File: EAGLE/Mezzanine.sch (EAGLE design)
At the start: 11 parts

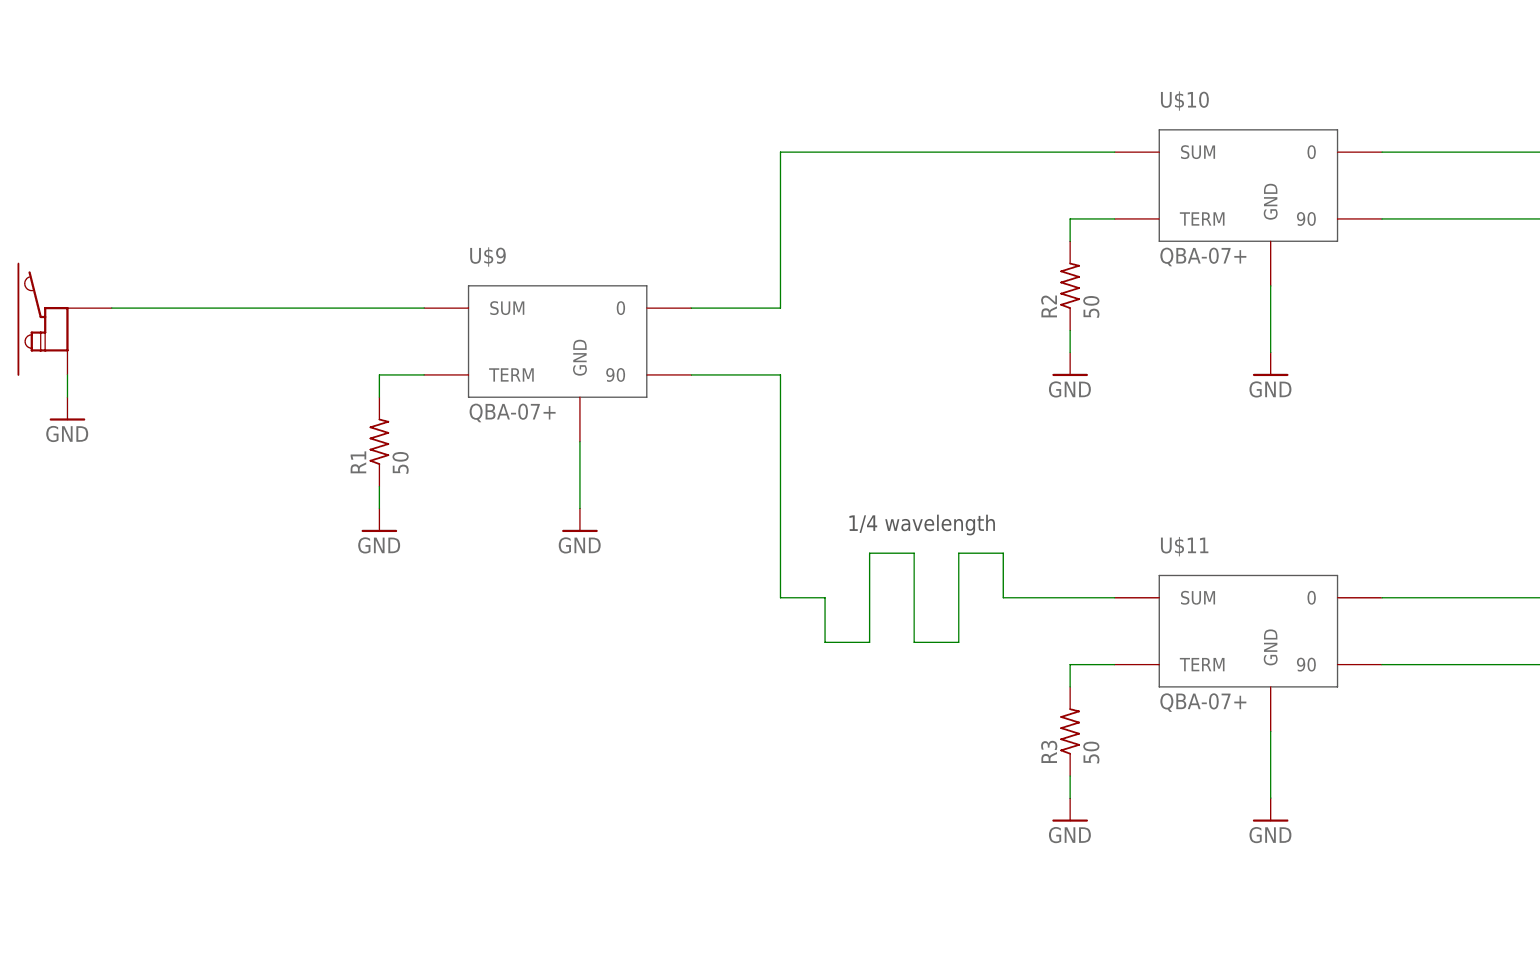
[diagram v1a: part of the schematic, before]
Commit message: Updated QBA footprints to have no solder mask in order to generate the correct solder paste stencils.
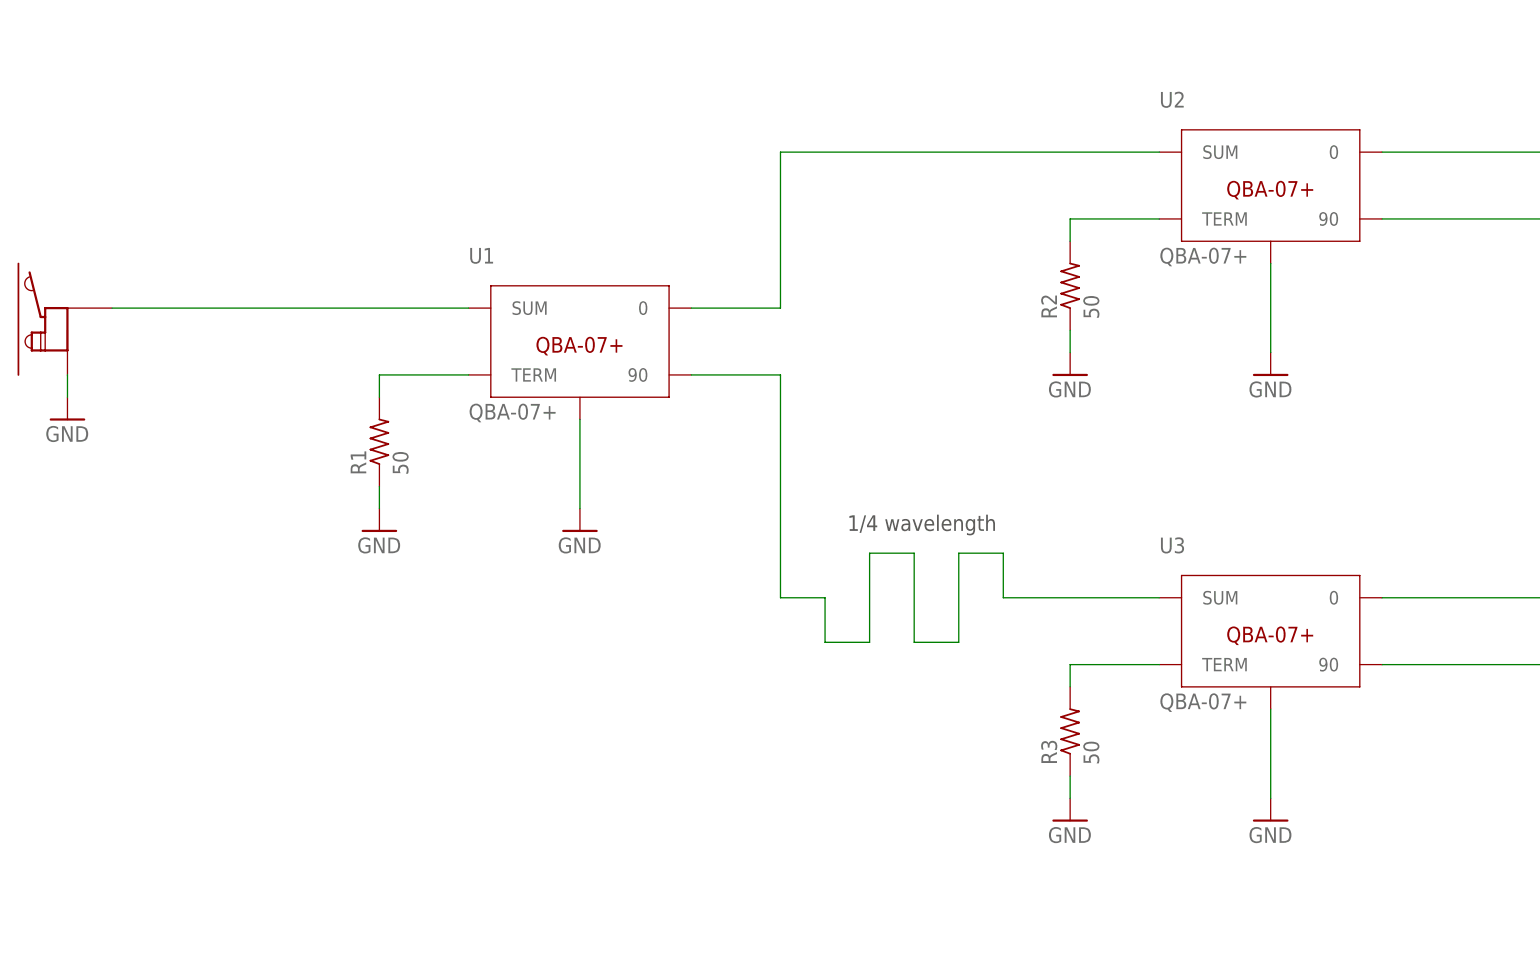
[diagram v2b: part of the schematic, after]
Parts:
- removed U$10, U$11, U$9: QBA-07+, Mini-Circuits-QBA-07+_Phase-shifter:QBA-07+
- added U1, U2, U3: QBA-07+, U-MiniCirc-QBA-07+_Phase-shifter:QBA-07+
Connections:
- net GND: now also U1.GND, U2.GND, U3.GND; no longer U$10.GND, U$11.GND, U$9.GND
- net N$1: now also U1.SUM; no longer U$9.SUM
- net N$2: now also U1.0, U2.SUM; no longer U$10.SUM, U$9.0
- net N$3: now also U1.TERM; no longer U$9.TERM
- net N$4: now also U2.TERM; no longer U$10.TERM
- net N$5: now also U1.90, U3.SUM; no longer U$11.SUM, U$9.90
- net N$6: now also U3.TERM; no longer U$11.TERM
- net UHF_0: now also U2.0; no longer U$10.0
- net UHF_180: now also U3.0; no longer U$11.0
- net UHF_270: now also U3.90; no longer U$11.90
- net UHF_90: now also U2.90; no longer U$10.90
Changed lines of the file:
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@@
 <?xml version="1.0" encoding="utf-8"?>
 <!DOCTYPE eagle SYSTEM "eagle.dtd">
-<eagle version="9.6.2">
+<eagle version="9.6.1">
 <drawing>
 <settings>
@@
 <parts>
 <part name="FRAME1" library="frames" library_urn="urn:adsk.eagle:library:229" deviceset="FRAME_A_L" device=""/>
-<part name="U$9" library="Mini-Circuits-QBA-07+_Phase-shifter" deviceset="QBA-07+" device=""/>
-<part name="U$10" library="Mini-Circuits-QBA-07+_Phase-shifter" deviceset="QBA-07+" device=""/>
-<part name="U$11" library="Mini-Circuits-QBA-07+_Phase-shifter" deviceset="QBA-07+" device=""/>
+<part name="U1" library="U-MiniCirc-QBA-07+_Phase-shifter" deviceset="QBA-07+" device=""/>
+<part name="U2" library="U-MiniCirc-QBA-07+_Phase-shifter" deviceset="QBA-07+" device=""/>
+<part name="U3" library="U-MiniCirc-QBA-07+_Phase-shifter" deviceset="QBA-07+" device=""/>
 <part name="GND1" library="supply1" library_urn="urn:adsk.eagle:library:371" deviceset="GND" device=""/>
 <part name="GND2" library="supply1" library_urn="urn:adsk.eagle:library:371" deviceset="GND" device=""/>
@@
 <attribute name="DRAWING_NAME" x="190.5" y="19.05" size="2.54" layer="94"/>
 </instance>
-<instance part="U$9" gate="G$1" x="91.44" y="127" smashed="yes">
+<instance part="U1" gate="G$1" x="91.44" y="127" smashed="yes">
 <attribute name="NAME" x="78.74" y="134.62" size="1.778" layer="95"/>
 <attribute name="VALUE" x="78.74" y="116.84" size="1.778" layer="96"/>
 </instance>
-<instance part="U$10" gate="G$1" x="170.18" y="144.78" smashed="yes">
+<instance part="U2" gate="G$1" x="170.18" y="144.78" smashed="yes">
 <attribute name="NAME" x="157.48" y="152.4" size="1.778" layer="95"/>
 <attribute name="VALUE" x="157.48" y="134.62" size="1.778" layer="96"/>
 </instance>
-<instance part="U$11" gate="G$1" x="170.18" y="93.98" smashed="yes">
+<instance part="U3" gate="G$1" x="170.18" y="93.98" smashed="yes">
 <attribute name="NAME" x="157.48" y="101.6" size="1.778" layer="95"/>
 <attribute name="VALUE" x="157.48" y="83.82" size="1.778" layer="96"/>
@@
 <net name="N$1" class="1">
 <segment>
-<pinref part="U$9" gate="G$1" pin="SUM"/>
-<wire x1="38.1" y1="129.54" x2="73.66" y2="129.54" width="0.1524" layer="91"/>
+<pinref part="U1" gate="G$1" pin="SUM"/>
+<wire x1="38.1" y1="129.54" x2="78.74" y2="129.54" width="0.1524" layer="91"/>
 <pinref part="U$1" gate="G$1" pin="P$1"/>
 </segment>
@@
 <net name="N$2" class="1">
 <segment>
-<pinref part="U$9" gate="G$1" pin="0"/>
+<pinref part="U1" gate="G$1" pin="0"/>
 <wire x1="104.14" y1="129.54" x2="114.3" y2="129.54" width="0.1524" layer="91"/>
 <wire x1="114.3" y1="129.54" x2="114.3" y2="147.32" width="0.1524" layer="91"/>
-<pinref part="U$10" gate="G$1" pin="SUM"/>
-<wire x1="114.3" y1="147.32" x2="152.4" y2="147.32" width="0.1524" layer="91"/>
+<pinref part="U2" gate="G$1" pin="SUM"/>
+<wire x1="114.3" y1="147.32" x2="157.48" y2="147.32" width="0.1524" layer="91"/>
 </segment>
 </net>
 <net name="N$3" class="1">
 <segment>
-<pinref part="U$9" gate="G$1" pin="TERM"/>
-<wire x1="73.66" y1="121.92" x2="68.58" y2="121.92" width="0.1524" layer="91"/>
+<pinref part="U1" gate="G$1" pin="TERM"/>
+<wire x1="78.74" y1="121.92" x2="68.58" y2="121.92" width="0.1524" layer="91"/>
 <wire x1="68.58" y1="121.92" x2="68.58" y2="119.38" width="0.1524" layer="91"/>
 <pinref part="R1" gate="R" pin="2"/>
@@
 </segment>
 <segment>
-<pinref part="U$9" gate="G$1" pin="GND"/>
+<pinref part="U1" gate="G$1" pin="GND"/>
 <pinref part="GND1" gate="1" pin="GND"/>
-<wire x1="91.44" y1="114.3" x2="91.44" y2="106.68" width="0.1524" layer="91"/>
-</segment>
-<segment>
-<pinref part="U$10" gate="G$1" pin="GND"/>
+<wire x1="91.44" y1="116.84" x2="91.44" y2="106.68" width="0.1524" layer="91"/>
+</segment>
+<segment>
+<pinref part="U2" gate="G$1" pin="GND"/>
 <pinref part="GND2" gate="1" pin="GND"/>
-<wire x1="170.18" y1="132.08" x2="170.18" y2="124.46" width="0.1524" layer="91"/>
+<wire x1="170.18" y1="134.62" x2="170.18" y2="124.46" width="0.1524" layer="91"/>
 </segment>
 <segment>
@@
 </segment>
 <segment>
-<pinref part="U$11" gate="G$1" pin="GND"/>
+<pinref part="U3" gate="G$1" pin="GND"/>
 <pinref part="GND3" gate="1" pin="GND"/>
-<wire x1="170.18" y1="81.28" x2="170.18" y2="73.66" width="0.1524" layer="91"/>
+<wire x1="170.18" y1="83.82" x2="170.18" y2="73.66" width="0.1524" layer="91"/>
 </segment>
 <segment>
@@
 <net name="N$4" class="1">
 <segment>
-<pinref part="U$10" gate="G$1" pin="TERM"/>
-<wire x1="152.4" y1="139.7" x2="147.32" y2="139.7" width="0.1524" layer="91"/>
+<pinref part="U2" gate="G$1" pin="TERM"/>
+<wire x1="157.48" y1="139.7" x2="147.32" y2="139.7" width="0.1524" layer="91"/>
 <wire x1="147.32" y1="139.7" x2="147.32" y2="137.16" width="0.1524" layer="91"/>
 <pinref part="R2" gate="R" pin="2"/>
@@
 <net name="N$5" class="1">
 <segment>
-<pinref part="U$11" gate="G$1" pin="SUM"/>
-<wire x1="152.4" y1="96.52" x2="139.7" y2="96.52" width="0.1524" layer="91"/>
+<pinref part="U3" gate="G$1" pin="SUM"/>
+<wire x1="157.48" y1="96.52" x2="139.7" y2="96.52" width="0.1524" layer="91"/>
 <wire x1="139.7" y1="96.52" x2="139.7" y2="101.6" width="0.1524" layer="91"/>
 <wire x1="139.7" y1="101.6" x2="134.62" y2="101.6" width="0.1524" layer="91"/>
@@
 <wire x1="119.38" y1="96.52" x2="114.3" y2="96.52" width="0.1524" layer="91"/>
 <wire x1="114.3" y1="96.52" x2="114.3" y2="121.92" width="0.1524" layer="91"/>
-<pinref part="U$9" gate="G$1" pin="90"/>
+<pinref part="U1" gate="G$1" pin="90"/>
 <wire x1="114.3" y1="121.92" x2="104.14" y2="121.92" width="0.1524" layer="91"/>
 </segment>
@@
 <net name="N$6" class="1">
 <segment>
-<pinref part="U$11" gate="G$1" pin="TERM"/>
-<wire x1="152.4" y1="88.9" x2="147.32" y2="88.9" width="0.1524" layer="91"/>
+<pinref part="U3" gate="G$1" pin="TERM"/>
+<wire x1="157.48" y1="88.9" x2="147.32" y2="88.9" width="0.1524" layer="91"/>
 <wire x1="147.32" y1="88.9" x2="147.32" y2="86.36" width="0.1524" layer="91"/>
 <pinref part="R3" gate="R" pin="2"/>
@@
 <net name="UHF_0" class="1">
 <segment>
-<pinref part="U$10" gate="G$1" pin="0"/>
+<pinref part="U2" gate="G$1" pin="0"/>
 <wire x1="182.88" y1="147.32" x2="213.36" y2="147.32" width="0.1524" layer="91"/>
 <label x="203.2" y="147.32" size="1.778" layer="95"/>
@@
 <net name="UHF_90" class="1">
 <segment>
-<pinref part="U$10" gate="G$1" pin="90"/>
+<pinref part="U2" gate="G$1" pin="90"/>
 <wire x1="182.88" y1="139.7" x2="213.36" y2="139.7" width="0.1524" layer="91"/>
 <label x="203.2" y="139.7" size="1.778" layer="95"/>
@@
 <net name="UHF_270" class="1">
 <segment>
-<pinref part="U$11" gate="G$1" pin="90"/>
+<pinref part="U3" gate="G$1" pin="90"/>
 <label x="203.2" y="88.9" size="1.778" layer="95"/>
 <wire x1="182.88" y1="88.9" x2="223.52" y2="88.9" width="0.1524" layer="91"/>
@@
 <net name="UHF_180" class="1">
 <segment>
-<pinref part="U$11" gate="G$1" pin="0"/>
+<pinref part="U3" gate="G$1" pin="0"/>
 <wire x1="182.88" y1="96.52" x2="213.36" y2="96.52" width="0.1524" layer="91"/>
 <label x="203.2" y="96.52" size="1.778" layer="95"/>
